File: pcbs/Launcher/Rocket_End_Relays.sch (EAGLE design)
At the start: 32 parts, among them IC1 7805TV, K4 LD105, K5 LD105, K6 LD105, K7 LD105, T1 BC547, T2 BC547, T3 BC547, T4 BC547, T5 BC547, U1 ARDUINO-MEGAPRO-5V, X1 22-23-2041, X2 22-23-2041, X4 22-23-2021, X5 22-23-2021, X6 22-23-2021

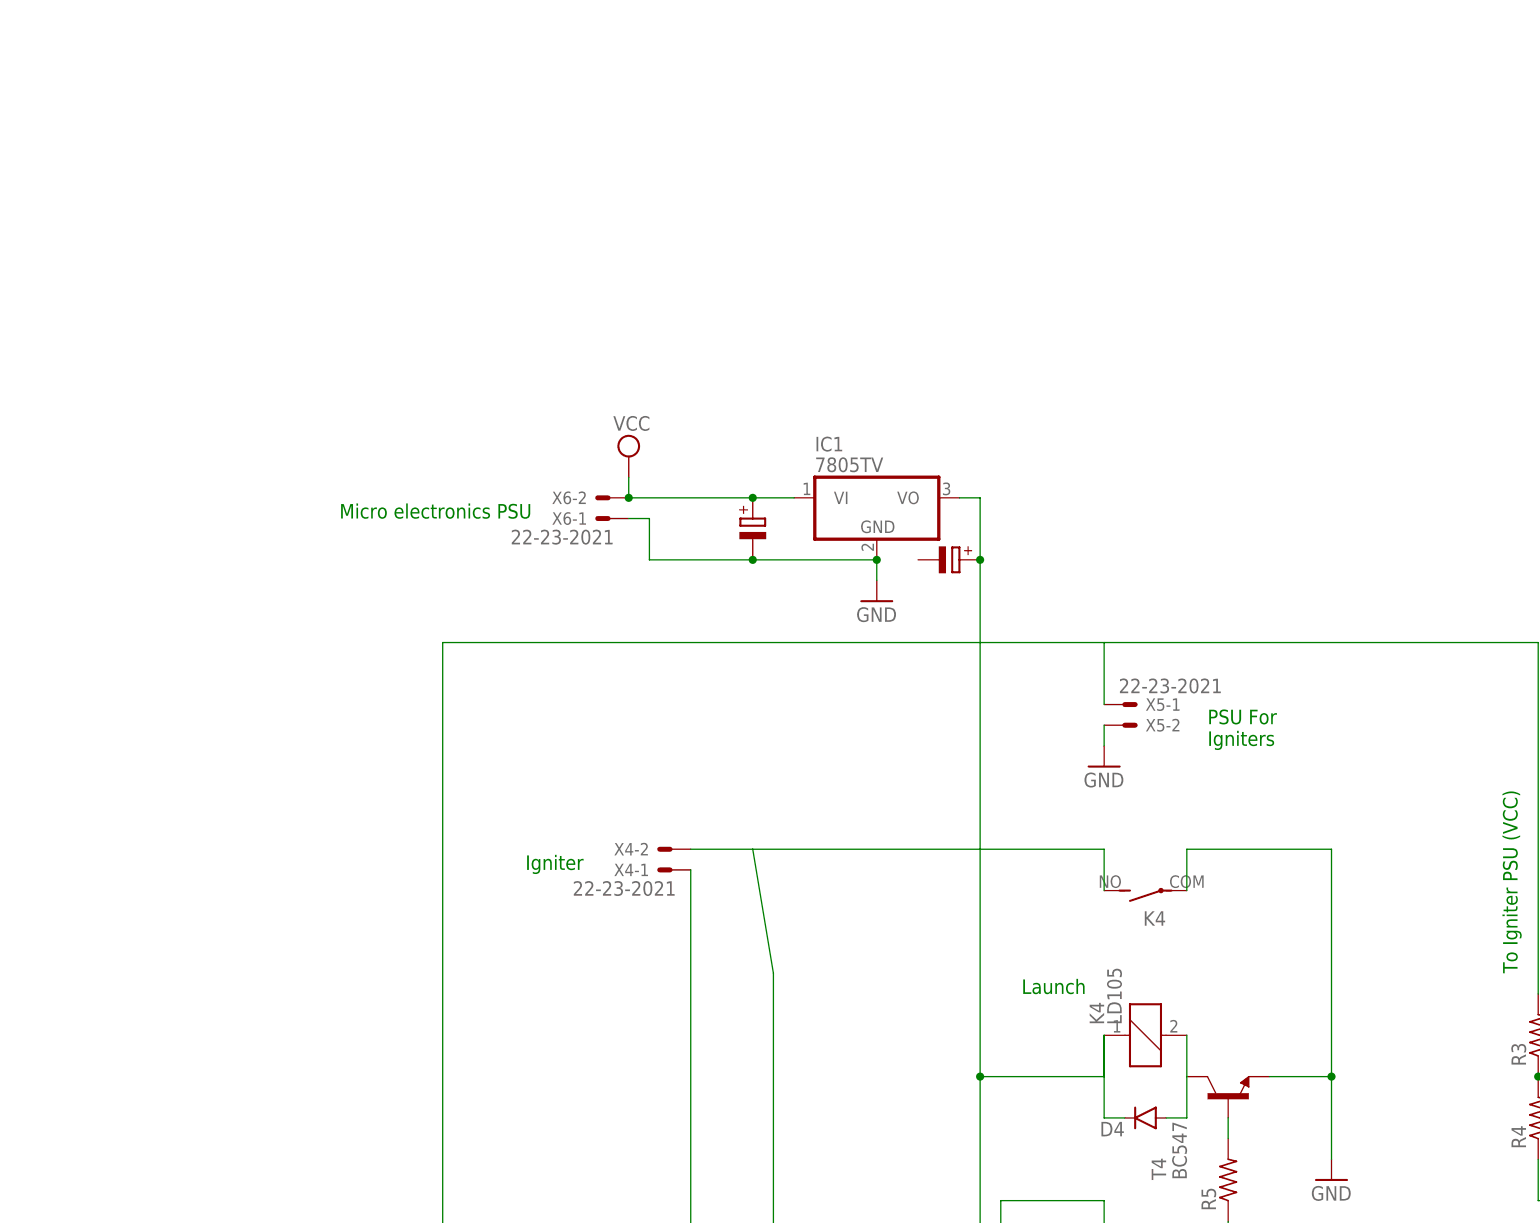
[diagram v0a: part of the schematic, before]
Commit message: * Adding Switch Mode PSU which will be used for relays and   for the RFD900a radio modem.
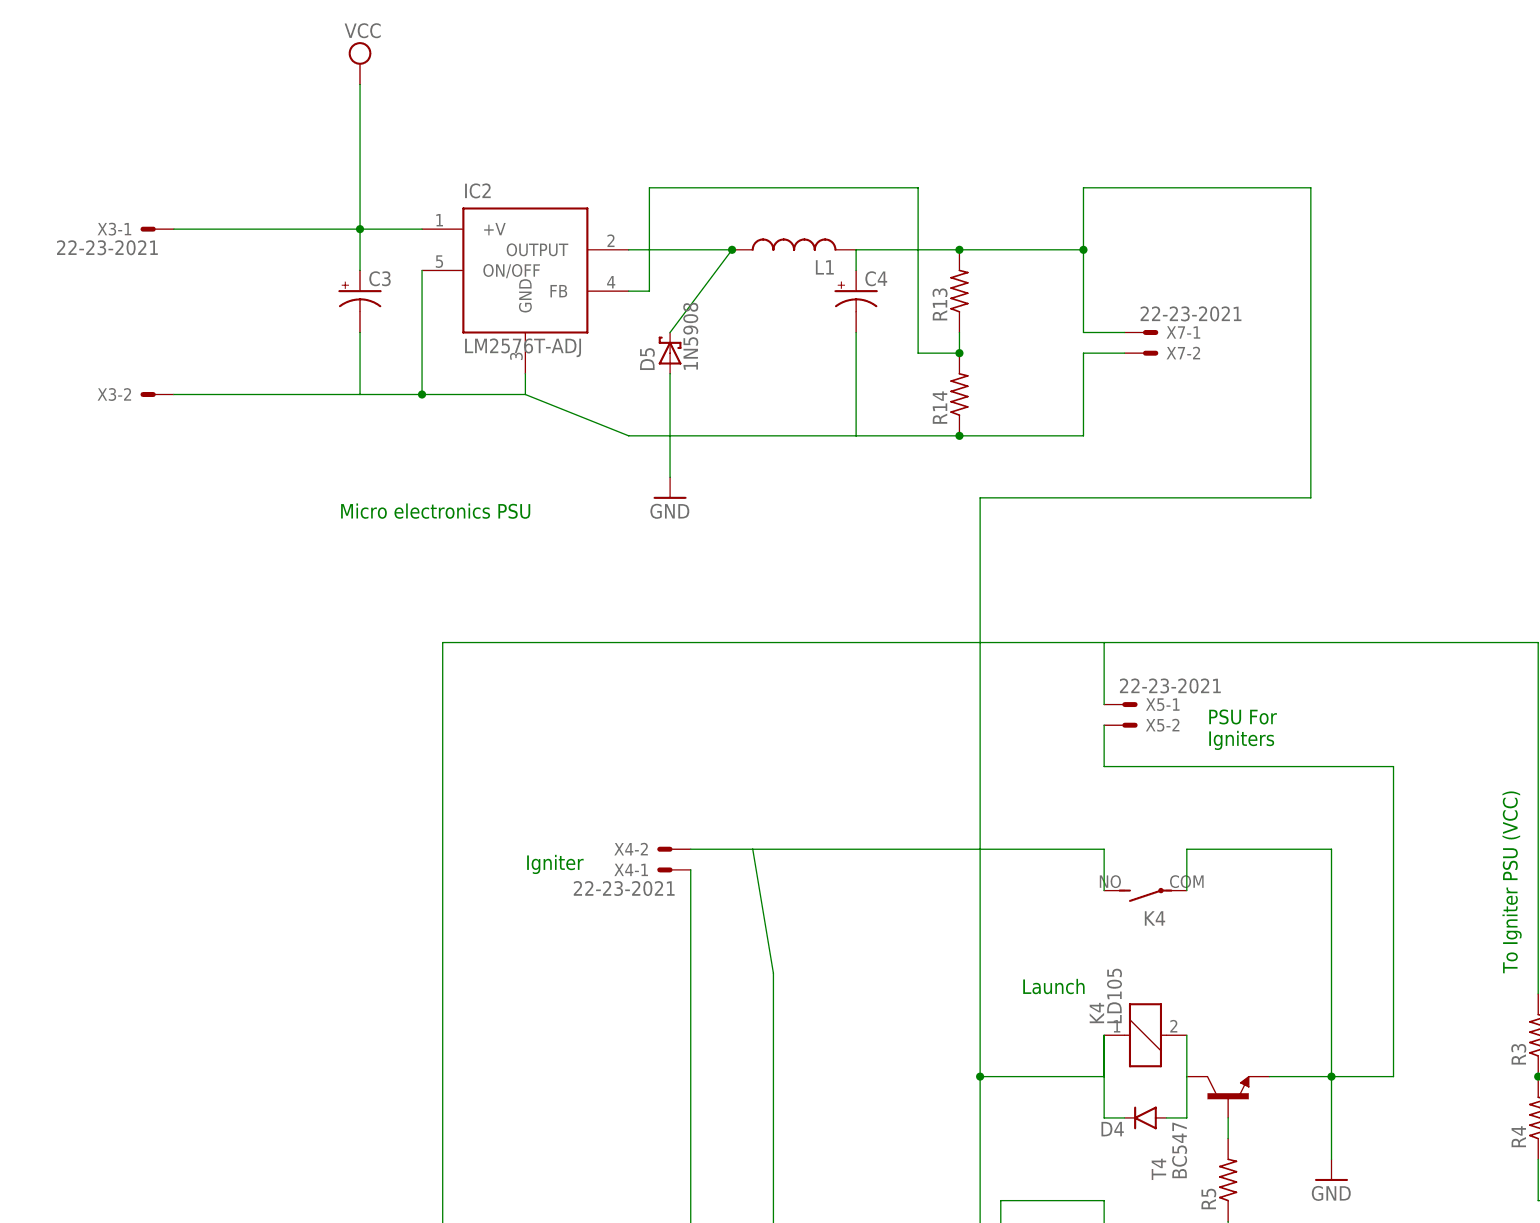
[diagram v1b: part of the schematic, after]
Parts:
- removed IC1: 7805TV, linear:7805TV
- removed X6: 22-23-2021, con-molex:22-23-2021
- added C3, C4: (no value), rcl:CPOL-USE2-4
- added D5: 1N5908, diode:1N5908
- added IC2: LM2576T-ADJ, LM2576:LM2576T-ADJ
- added L1: (no value), resistor:L-USTJ3-U1
- added R13, R14: (no value), rcl:R-US_0204/5
- added X3, X7: 22-23-2021, con-molex:22-23-2021
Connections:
- new net N$36: D5.C, IC2.OUTPUT, L1.1
- new net N$37: IC2.FB, R13.1, R14.2
- net GND: now also C3.-, C4.-, D5.A, IC2.GND, IC2.ON/OFF, R14.1, X3-2.S, X7-2.S; no longer IC1.GND, X6-1.S
- net N$5: now also C4.+, L1.2, R13.2, X7-1.S; no longer IC1.VO
- net VCC: now also C3.+, IC2.+V, X3-1.S; no longer IC1.VI, X6-2.S

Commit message: * Moving relay and other components over to make more room for Inductor * Moving the Lm2576 up and right to fit in with new Inductor
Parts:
- L1: device resistor:L-USTJ3-U1 -> resistor:L-USTJ4-U1
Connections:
- net GND renamed N$33
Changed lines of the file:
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@@
 <part name="C3" library="rcl" deviceset="CPOL-US" device="E2-4"/>
 <part name="C4" library="rcl" deviceset="CPOL-US" device="E2-4"/>
-<part name="L1" library="resistor" deviceset="L-US" device="TJ3-U1"/>
+<part name="L1" library="resistor" deviceset="L-US" device="TJ4-U1"/>
 <part name="R13" library="rcl" deviceset="R-US_" device="0204/5"/>
 <part name="R14" library="rcl" deviceset="R-US_" device="0204/5"/>
@@
 </segment>
 </net>
-<net name="GND" class="0">
+<net name="N$33" class="0">
 <segment>
 <pinref part="T2" gate="G$1" pin="E"/>

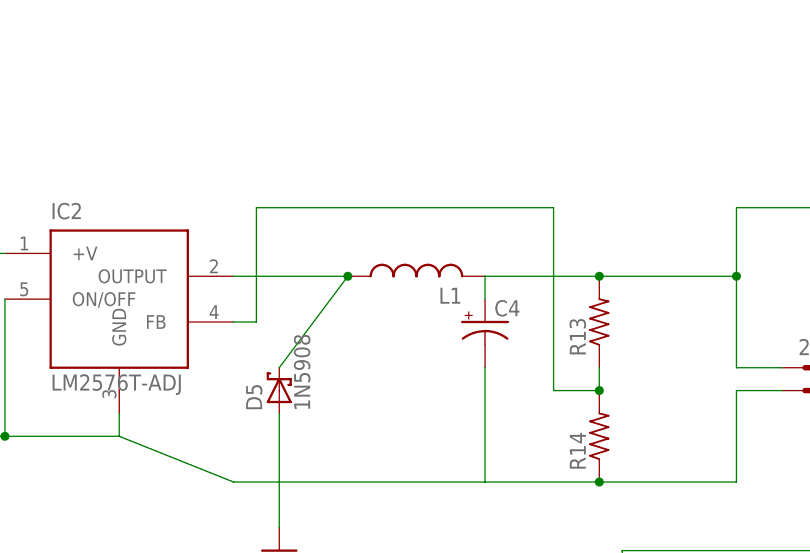
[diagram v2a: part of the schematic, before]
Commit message: * Trying to remove some top tracks.
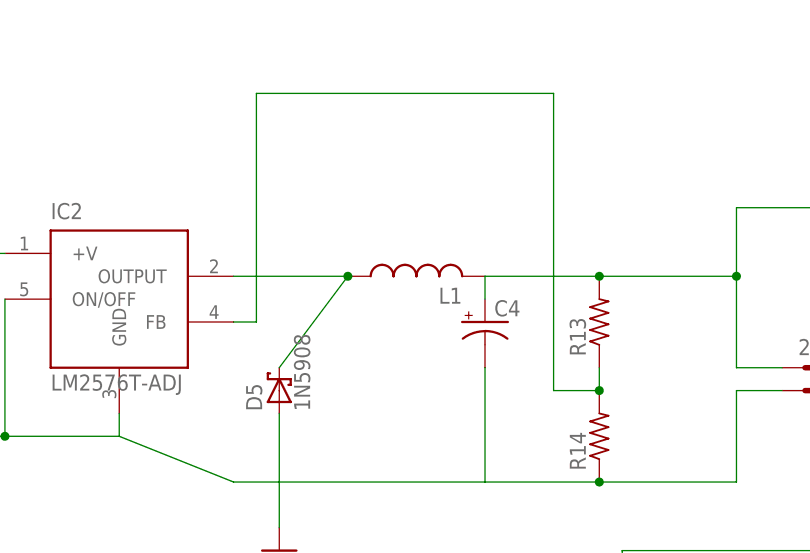
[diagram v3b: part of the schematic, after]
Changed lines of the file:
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@@
 <pinref part="IC2" gate="G$1" pin="FB"/>
 <wire x1="-116.84" y1="165.1" x2="-114.3" y2="165.1" width="0.1524" layer="91"/>
-<wire x1="-114.3" y1="165.1" x2="-114.3" y2="177.8" width="0.1524" layer="91"/>
-<wire x1="-114.3" y1="177.8" x2="-81.28" y2="177.8" width="0.1524" layer="91"/>
-<wire x1="-81.28" y1="177.8" x2="-81.28" y2="157.48" width="0.1524" layer="91"/>
+<wire x1="-114.3" y1="165.1" x2="-114.3" y2="190.5" width="0.1524" layer="91"/>
+<wire x1="-114.3" y1="190.5" x2="-81.28" y2="190.5" width="0.1524" layer="91"/>
+<wire x1="-81.28" y1="190.5" x2="-81.28" y2="157.48" width="0.1524" layer="91"/>
 <wire x1="-81.28" y1="157.48" x2="-76.2" y2="157.48" width="0.1524" layer="91"/>
 <junction x="-76.2" y="157.48"/>

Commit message: * Added Arduino code for launcher code
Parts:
- R10: device resistor:R-US_0207/7 -> rcl:R-US_0207/7
- R13, R14: device rcl:R-US_0204/5 -> resistor:R-US_0207/7
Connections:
- removed net N$28: U1.5V@1, X1-3.S, X2-3.S
- net N$23: now also R12.2, U1.5V@1, X1-3.S, X2-3.S; no longer R12.1, T5.C
- net N$26: now also R12.1, T5.C; no longer R10.2, T5.E
- net N$31: now also R10.2
- net N$33: now also T5.E
- net N$5: no longer R12.2
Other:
- moved on the sheet: R10

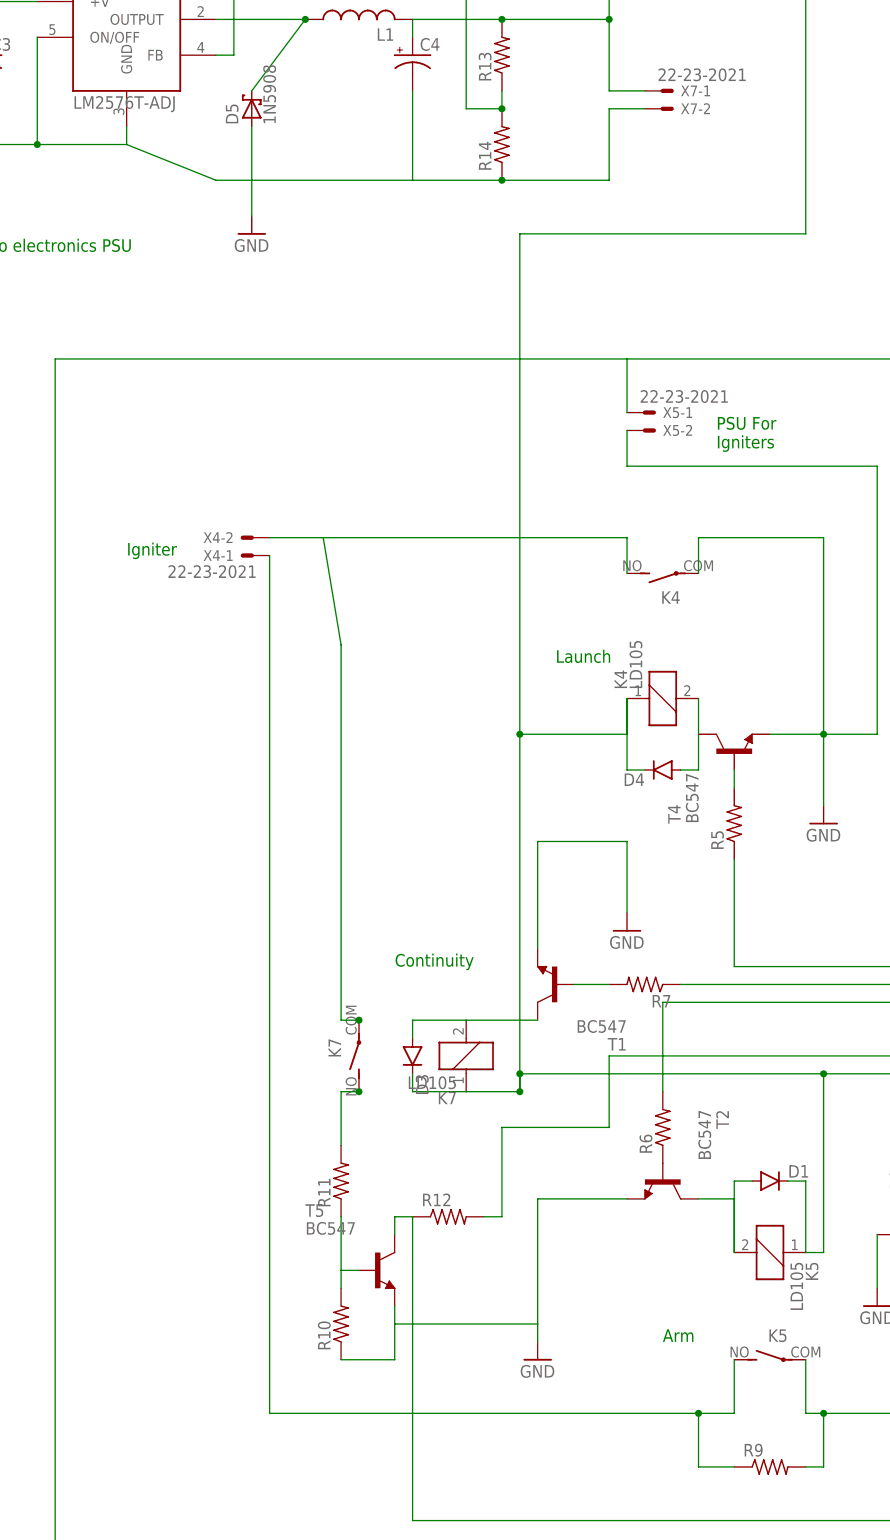
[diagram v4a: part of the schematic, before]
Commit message: * Cleaning up board with curved tracks * Putting in two screw in terminal blocks for Igniter PSU   and wires to igniter!
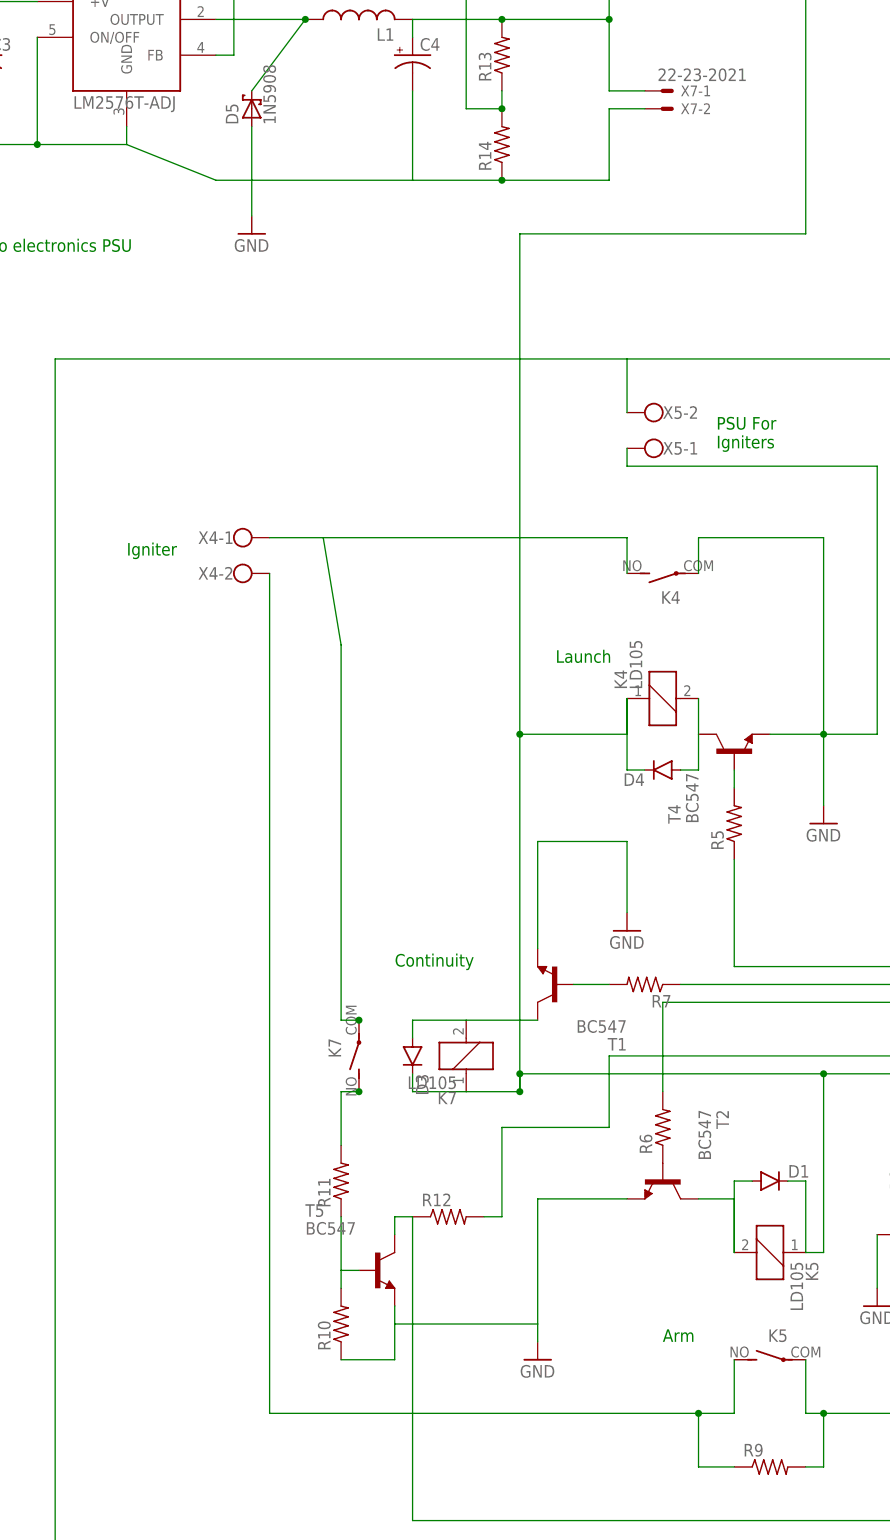
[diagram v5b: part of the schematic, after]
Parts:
- X4, X5: value 22-23-2021 -> (none); device con-molex:22-23-2021 -> con-wago-500:W237-102
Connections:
- net N$15: now also X4-1.KL; no longer X4-2.S
- net N$17: now also X4-2.KL; no longer X4-1.S
- net N$29: now also X5-2.KL; no longer X5-1.S
- net N$33: now also X5-1.KL; no longer X5-2.S
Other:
- moved on the sheet: X4-1, X4-2, X5-1, X5-2
